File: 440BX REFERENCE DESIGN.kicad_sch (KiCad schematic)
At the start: 2 parts, among them U1001 SN74HC10DR-separate, U1002 7407

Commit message: fixed up cover sheet
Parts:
- removed U1001: SN74HC10DR-separate, symbol P2-3_era:SN74HC10DR-separate
- removed U1002: 7407, P2-3_ERA:NS14, symbol 74xx_IEEE:7407
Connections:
- no-connect marks 4 -> 0
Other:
- sheet HARDWARE MONITOR renamed LM79
- sheet PCI CONNECTORS renamed PCI CONNECTORS 1 & 2
- sheet PCI CONNECTORS1 renamed PCI CONNECTORS 3 & 4
- sheet PS2 CONNS renamed KEYBOARD MOUSE
- sheet SERIAL AND FLOPPY renamed SERIAL FLOPPY
- sheet ULTRAIO renamed ULTRA-IO.kicad_sch
- sheet VRMS renamed VRM
- note added: "COVER SHEET BLOCK DIAGRAM 2 SLOT 1 CONNECTOR CLOCK SYNTHESIZER 82443BX 6,7,8 DIMM SOCKETS 9,10,11 PIIX4E 12,13 ULTRA I/O AGP CONNECTOR PCI CONNECTORS ISA CONNECTORS IDE CONNECTORS USB CONNECTORS FLASH BIOS PARALLEL SERIAL/FLOPPY KEYBOARD/MOUSE VRM POWER CONNECTOR GTL+ TERMINATION PCI/AGP PULLUPS/PULLDOWNS ISA PULLUPS/PULLDOWNS 82443BX DECOUPLING BULK DECOUPLING TERMINATION DECOUPLING LM79 REVISIO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"
- note added: "Intel 100 MHz Pentium(tm) II processor/440BX AGPset Uniprocessor Customer Reference Schematics"
- note added: "PAGE"
- note added: "TITLE"
- note removed: "82443BX"
- note removed: "AGP"
- note removed: "BIOS"
- note removed: "BULK DECOUPLING"
- note removed: "CLOCK"
- note removed: "COM/FLOPPY"
- note removed: "DIMM"
- note removed: "GTL+ TERMINATION"
- note removed: "HARDWARE MONITOR"
- note removed: "IDE"
- note removed: "ISA"
- note removed: "ISA PULLUP-DOWNS"
- note removed: "PARALLEL"
- note removed: "PCI-AGP PULLUPS-DOWNS"
- note removed: "PCI1"
- note removed: "PCI2"
- note removed: "PII4XE"
- note removed: "PS2 CONNS"
- note removed: "Power Connector & Misc"
- note removed: "RAM, CLOCK, CHIPSET DECOUPLING"
- note removed: "SLOT 1"
- note removed: "TERMINATION DECOUPLING"
- note removed: "ULTRAIO"
- note removed: "USB"
- note removed: "VRMS"
- title: (none) -> Intel 100MHz Pentium(tm) II processor/440BX AGPset Uni-Processor Cover Sheet

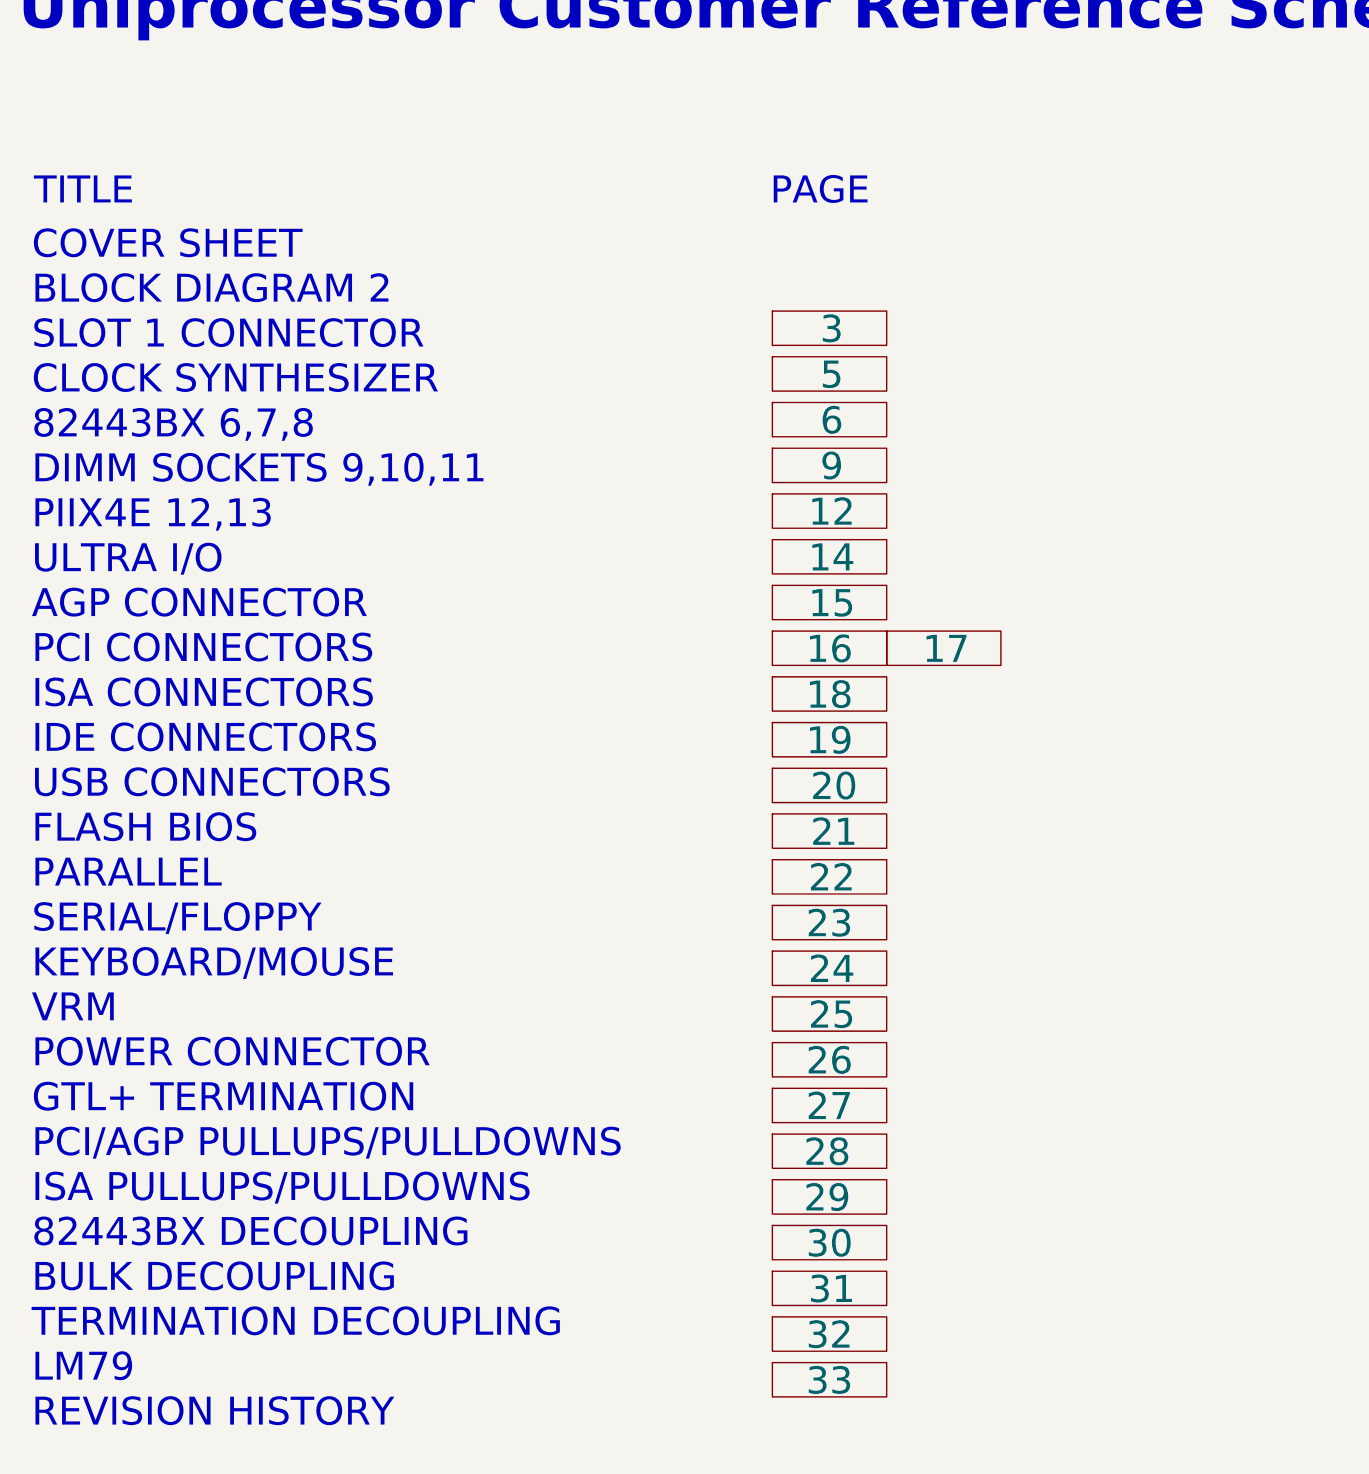
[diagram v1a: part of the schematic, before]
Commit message: improved Cover Sheet, BLOCK DIAGRAM from PDF thru SVG import
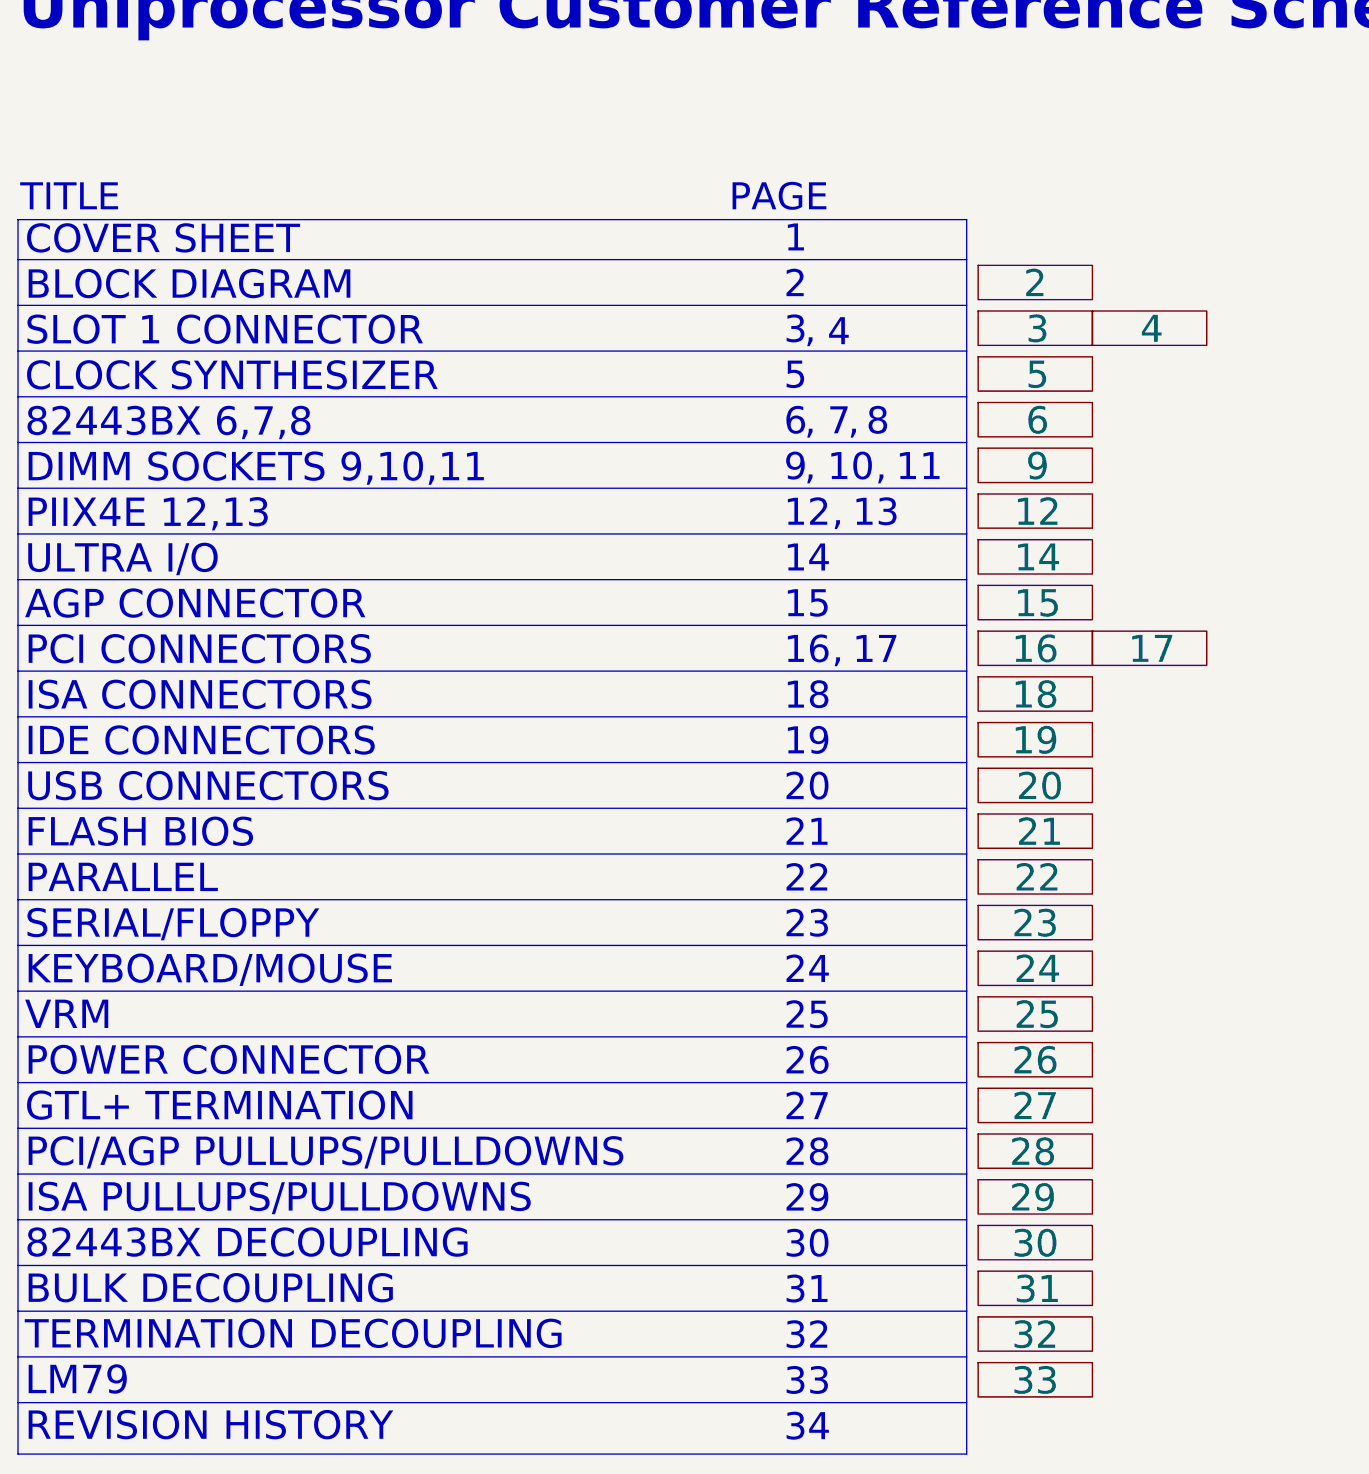
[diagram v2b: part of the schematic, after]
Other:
- sheet SLOT 1 CONNECTOR renamed SLOT 1 (PART I)
- added sheet BLOCK DIAGRAM (BLOCK DIAGRAM.kicad_sch)
- added sheet SLOT 1 (PART II) (SLOT 1 CONNECTOR.kicad_sch)
- note added: ","
- note added: "1"
- note added: "10"
- note added: "11"
- note added: "12"
- note added: "13"
- note added: "14"
- note added: "15"
- note added: "16"
- note added: "17"
- note added: "18"
- note added: "19"
- note added: "2"
- note added: "20"
- note added: "21"
- note added: "22"
- note added: "23"
- note added: "24"
- note added: "25"
- note added: "26"
- note added: "27"
- note added: "28"
- note added: "29"
- note added: "3"
- note added: "30"
- note added: "31"
- note added: "32"
- note added: "33"
- note added: "34"
- note added: "4"
- note added: "5"
- note added: "6"
- note added: "7"
- note added: "8"
- note added: "9"
- note added: "COVER SHEET BLOCK DIAGRAM SLOT 1 CONNECTOR CLOCK SYNTHESIZER 82443BX 6,7,8 DIMM SOCKETS 9,10,11 PIIX4E 12,13 ULTRA I/O AGP CONNECTOR PCI CONNECTORS ISA CONNECTORS IDE CONNECTORS USB CONNECTORS FLASH BIOS PARALLEL SERIAL/FLOPPY KEYBOARD/MOUSE VRM POWER CONNECTOR GTL+ TERMINATION PCI/AGP PULLUPS/PULLDOWNS ISA PULLUPS/PULLDOWNS 82443BX DECOUPLING BULK DECOUPLING TERMINATION DECOUPLING LM79 REVISION 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"
- note removed: "COVER SHEET BLOCK DIAGRAM 2 SLOT 1 CONNECTOR CLOCK SYNTHESIZER 82443BX 6,7,8 DIMM SOCKETS 9,10,11 PIIX4E 12,13 ULTRA I/O AGP CONNECTOR PCI CONNECTORS ISA CONNECTORS IDE CONNECTORS USB CONNECTORS FLASH BIOS PARALLEL SERIAL/FLOPPY KEYBOARD/MOUSE VRM POWER CONNECTOR GTL+ TERMINATION PCI/AGP PULLUPS/PULLDOWNS ISA PULLUPS/PULLDOWNS 82443BX DECOUPLING BULK DECOUPLING TERMINATION DECOUPLING LM79 REVISIO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"

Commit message: Page 3, 4 completed
perfect 1:1 symbols added: Slot1, MAX1617, Jumper
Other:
- sheet SLOT 1 (PART II): file SLOT 1 CONNECTOR.kicad_sch -> SLOT 1 CONNECTOR1.kicad_sch
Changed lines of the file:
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@@
 			)
 		)
-		(property "Sheetfile" "SLOT 1 CONNECTOR.kicad_sch"
+		(property "Sheetfile" "SLOT 1 CONNECTOR1.kicad_sch"
 			(at 148.59 66.6246 0)
 			(effects
